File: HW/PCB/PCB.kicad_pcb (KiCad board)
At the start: 2 copper layers, 66.7 x 44 mm, 54 parts, among them J1 USB4105-GF-A, J4 Micro_SD_Card_Det_Hirose_DM3AT, Q1 2PC4081R, Q2 2PC4081R, SW1 ssss213202, SW2 SKRPACE010, SW3 SKRPACE010, U1 BME280, U2 FT231XS, U3 LT1963ES8-3.3, U4 ESP32-S3-WROOM-1, U5 SCD40, U6 AQM0802A-RN-GBW, U7 TPS2065DDBVR, Y1 FC-135

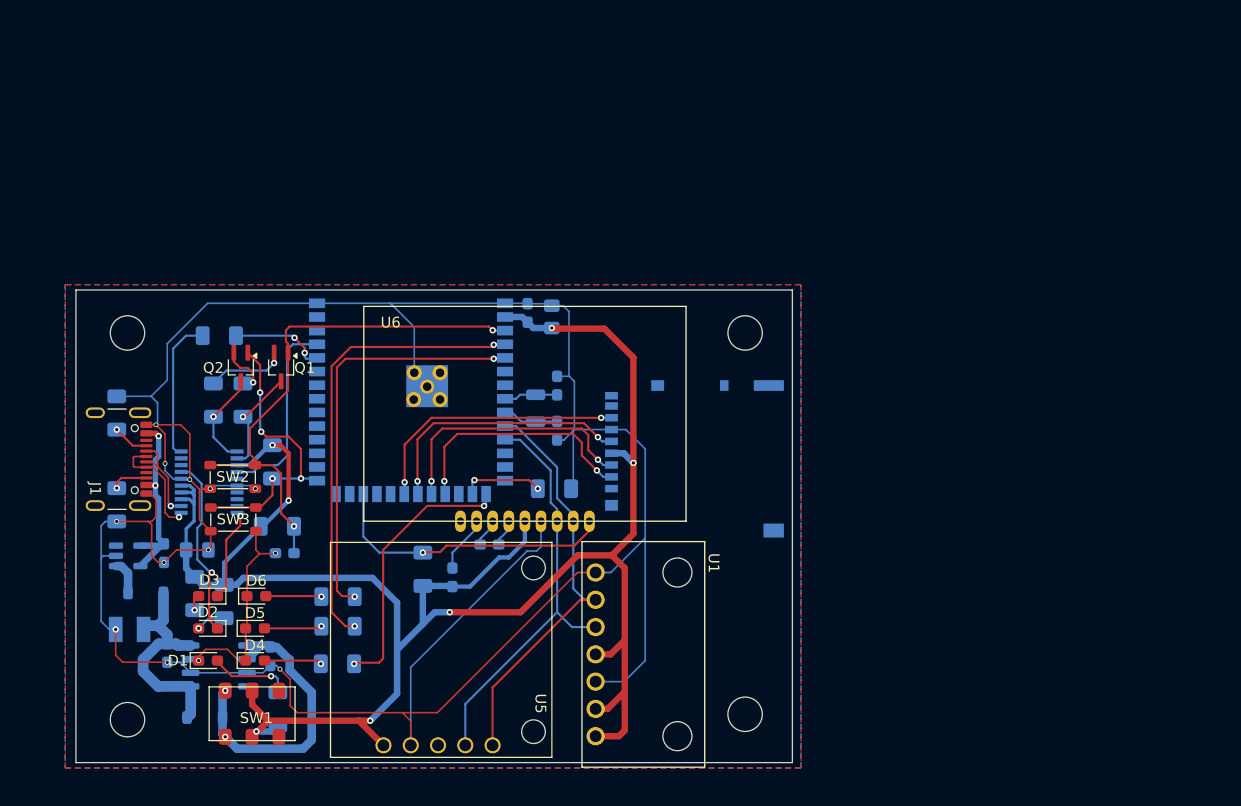
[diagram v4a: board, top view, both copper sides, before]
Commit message: add e-paper module
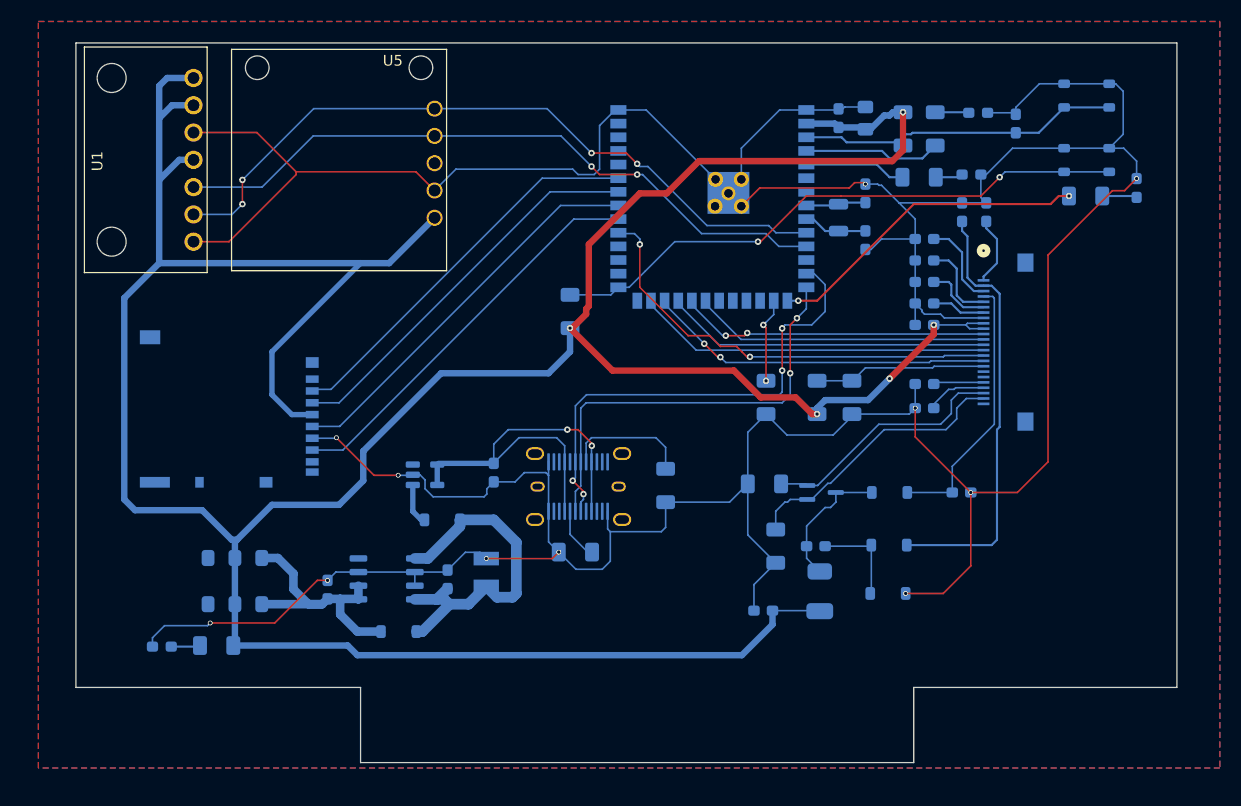
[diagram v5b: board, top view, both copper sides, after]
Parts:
- removed H1, H2, H3, H4: M3_MountHoll, MountingHole:MountingHole_3.2mm_M3
- removed Q1: 2PC4081R, Package_TO_SOT_SMD:SOT-323_SC-70_Handsoldering
- removed R12, R8: 10K, Resistor_SMD:R_1206_3216Metric_Pad1.30x1.75mm_HandSolder
- removed U6: AQM0802A-RN-GBW, mylib:AQM0802A-RN-GBW
- added C13: 4.7uF, Capacitor_SMD:C_0603_1608Metric_Pad1.08x0.95mm_HandSolder, B.Cu at (167.5, 67.2)
- added C15: 4.7uF, Capacitor_SMD:C_0603_1608Metric_Pad1.08x0.95mm_HandSolder, B.Cu at (167.5, 65.2)
- added C16: 4.7uF, Capacitor_SMD:C_0603_1608Metric_Pad1.08x0.95mm_HandSolder, B.Cu at (171.0, 62.8)
- added C17: 1uF, Capacitor_SMD:C_0603_1608Metric_Pad1.08x0.95mm_HandSolder, B.Cu at (173.2, 62.8)
- added C18: 4.7uF, Capacitor_SMD:C_0603_1608Metric_Pad1.08x0.95mm_HandSolder, B.Cu at (152.5, 99.8)
- added C19: 1uF, Capacitor_SMD:C_0603_1608Metric_Pad1.08x0.95mm_HandSolder, B.Cu at (157.4, 93.8)
- added C20: 4.7uF, Capacitor_SMD:C_0603_1608Metric_Pad1.08x0.95mm_HandSolder, B.Cu at (170.9, 88.8)
- added C21: 4.7uF, Capacitor_SMD:C_0603_1608Metric_Pad1.08x0.95mm_HandSolder, B.Cu at (167.5, 81.0)
- added C22: 1uF, Capacitor_SMD:C_0603_1608Metric_Pad1.08x0.95mm_HandSolder, B.Cu at (167.5, 69.2)
- added D9: RB161MM-20, Diode_SMD:D_SOD-123, B.Cu at (164.1, 98.2)
- added L1: 10uH, mylib:AMP10420ED, B.Cu at (157.8, 98.0)
- C3: value 0.1uF -> 4.7uF; footprint Capacitor_SMD:C_0805_2012Metric_Pad1.18x1.45mm_HandSolder -> Capacitor_SMD:C_0603_1608Metric_Pad1.08x0.95mm_HandSolder
- D1, D4, D5, D6, SW1, SW2, SW3: moved to B.Cu
- D2, D3: value LED -> RB161MM-20; footprint LED_SMD:LED_0603_1608Metric_Pad1.05x0.95mm_HandSolder -> Diode_SMD:D_SOD-123; moved to B.Cu
- J1: footprint Connector_USB:USB_C_Receptacle_GCT_USB4105-xx-A_16P_TopMnt_Horizontal -> mylib:USB-C31-S-VT-CS4-BK-PP-TR; moved to B.Cu
- Q2: value 2PC4081R -> SI1308EDL-T1-GE3; moved to B.Cu
- R3: value 470 -> 0.47
- R6: value 10K -> 3
- U2: value FT231XS -> E-Paper; footprint Package_SO:SSOP-20_3.9x8.7mm_P0.635mm -> XF2M-2415-1A:CONN_XF2M-2415-1A_OMR
- moved D4 93.1 mm to (187.2, 60.5), turned to -90 degrees
- moved SW2 87.1 mm to (182.6, 51.9)
- moved SW3 86.2 mm to (182.6, 57.9)
- moved D5 82.7 mm to (172.5, 53.5), turned to 180 degrees
- moved R13 82.1 mm to (182.5, 61.2), turned to 180 degrees
- moved C6 78.9 mm to (176.0, 54.5), turned to 90 degrees
- moved D6 77.3 mm to (171.9, 59.2), turned to 180 degrees
- moved U2 72.5 mm to (173.0, 80.6), turned to -90 degrees
- moved R14 72.4 mm to (168.5, 55.0), turned to -90 degrees
- moved C3 69.4 mm to (167.5, 78.8)
- moved R9 69.0 mm to (165.5, 55.0), turned to 90 degrees
- moved R15 66.7 mm to (167.0, 59.5), turned to 180 degrees
- moved D2 64.7 mm to (164.2, 88.8)
- moved R6 63.9 mm to (160.8, 80.0)
- moved D3 63.6 mm to (164.2, 93.8), turned to 0 degrees
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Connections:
- C10 pad 1: Net-(U6-CAP1N) -> GND
- C10 pad 2: Net-(U6-CAP1P) -> Net-(U2-VDD)
- C3 pad 1: +3V3 -> GND
- C3 pad 2: GND -> Net-(U2-VGH)
- C9 pad 1: +3V3 -> GND
- C9 pad 2: Net-(U6-VOUT) -> +3V3
- D2 pad 1: CBUS1 -> EPAPER_VGH
- D3 pad 1: CBUS2 -> Net-(D3-K)
- D3 pad 2: Net-(D3-A) -> EPAPER_VGL
- J1 pad A6: USB_DP -> ESP32_IO20
- J1 pad A7: USB_DM -> ESP32_IO19
- J1 pad B6: USB_DP -> ESP32_IO20
- J1 pad B7: USB_DM -> ESP32_IO19
- J4 pad 2: ESP32_IO10_SPI_CS -> ESP32_IO42_SD_CS
- J4 pad 3: ESP32_IO11_SPI_MOSI -> ESP32_IO41_SD_MOSI
- J4 pad 5: ESP32_IO12_SPI_SCK -> ESP32_IO40_SD_SCK
- J4 pad 7: ESP32_IO13_SPI_MISO -> ESP32_IO39_SD_MISO
- Q2 pad 1: ESP32_IO0 -> EPAPER_GDR
- Q2 pad 2: Net-(Q2-B) -> EPAPER_RESET
- Q2 pad 3: DTR -> Net-(D2-A)
- R3 pad 1: Net-(U2-TXD) -> EPAPER_RESET
- R3 pad 2: ESP32_RXD -> GND
- R5 pad 1: Net-(D2-A) -> EPAPER_GDR
- R5 pad 2: +3V3 -> GND
- R6 pad 1: Net-(D3-A) -> GND
- R6 pad 2: +3V3 -> Net-(U2-BS)
- R7 pad 1: Net-(Q1-B) -> +3V3
- R7 pad 2: DTR -> Net-(U2-BS)
- U2 pad 1: DTR -> unconnected-(U2-HLT_CTL-Pad1)
- U2 pad 10: CBUS2 -> ESP32_IO38_EPAPER_RST
- U2 pad 11: USB_DP -> ESP32_IO48_EPAPER_DC
- U2 pad 12: USB_DM -> ESP32_IO21_EPAPER_CS
- U2 pad 13: +3V3 -> ESP32_IO14_EPAPER_SCK
- U2 pad 14: +3V3 -> ESP32_IO13_EPAPER_MOSI
- U2 pad 16: GND -> +3V3
- U2 pad 17: CBUS1 -> GND
- U2 pad 18: unconnected-(U2-CBUS0-Pad18) -> Net-(U2-VDD)
- U2 pad 19: unconnected-(U2-CBUS3-Pad19) -> Net-(U2-VPP)
- U2 pad 2: RTS -> EPAPER_GDR
- U2 pad 20: Net-(U2-TXD) -> Net-(U2-VSH)
- U2 pad 3: +3V3 -> EPAPER_RESET
- U2 pad 4: ESP32_TXD -> Net-(U2-VGL)
- U2 pad 5: unconnected-(U2-~{RI}-Pad5) -> Net-(U2-VGH)
- U2 pad 6: GND -> unconnected-(U2-TSCL-Pad6)
- U2 pad 8: unconnected-(U2-~{DCD}-Pad8) -> Net-(U2-BS)
- U2 pad 9: unconnected-(U2-~{CTS}-Pad9) -> ESP32_IO47_EPAPER_BUSY
- U4 pad 13: unconnected-(U4-IO19-Pad13) -> ESP32_IO19
- U4 pad 14: unconnected-(U4-IO20-Pad14) -> ESP32_IO20
- U4 pad 18: ESP32_IO10_SPI_CS -> unconnected-(U4-IO10-Pad18)
- U4 pad 19: ESP32_IO11_SPI_MOSI -> unconnected-(U4-IO11-Pad19)
- U4 pad 20: ESP32_IO12_SPI_SCK -> unconnected-(U4-IO12-Pad20)
- U4 pad 21: ESP32_IO13_SPI_MISO -> ESP32_IO14_EPAPER_SCK
- U4 pad 22: unconnected-(U4-IO14-Pad22) -> ESP32_IO13_EPAPER_MOSI
- U4 pad 23: unconnected-(U4-IO21-Pad23) -> ESP32_IO21_EPAPER_CS
- U4 pad 24: ESP32_IO47 -> ESP32_IO47_EPAPER_BUSY
- U4 pad 25: unconnected-(U4-IO48-Pad25) -> ESP32_IO48_EPAPER_DC
- U4 pad 31: unconnected-(U4-IO38-Pad31) -> ESP32_IO38_EPAPER_RST
- U4 pad 32: unconnected-(U4-IO39-Pad32) -> ESP32_IO39_SD_MISO
- U4 pad 33: unconnected-(U4-IO40-Pad33) -> ESP32_IO40_SD_SCK
- U4 pad 34: unconnected-(U4-IO41-Pad34) -> ESP32_IO41_SD_MOSI
- U4 pad 35: unconnected-(U4-IO42-Pad35) -> ESP32_IO42_SD_CS
- U4 pad 36: ESP32_RXD -> unconnected-(U4-RXD0-Pad36)
- U4 pad 37: ESP32_TXD -> unconnected-(U4-TXD0-Pad37)
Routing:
- net +3V3: track 189.8 -> 323.8 mm, vias 7 -> 5
- net GND: track 284.7 -> 384.2 mm, vias 13 -> 11
- net ESP32_IO19: track 0.00 -> 45.5 mm, vias 0 -> 4
- net ESP32_IO38_EPAPER_RST: track 0.00 -> 41.5 mm, vias 0 -> 2
- net EPAPER_VGL: track 0.00 -> 40.7 mm
- net ESP32_IO20: track 0.00 -> 40.4 mm, vias 0 -> 2
- net ESP32_IO39_SD_MISO: track 0.00 -> 37.4 mm
- net ESP32_IO40_SD_SCK: track 0.00 -> 37.0 mm
- net ESP32_IO42_SD_CS: track 0.00 -> 36.7 mm
- net ESP32_IO41_SD_MOSI: track 0.00 -> 36.6 mm
- net ESP32_IO48_EPAPER_DC: track 0.00 -> 33.1 mm
- net ESP32_IO47_EPAPER_BUSY: track 0.00 -> 32.3 mm, vias 0 -> 2
- net ESP32_IO21_EPAPER_CS: track 0.00 -> 30.3 mm
- net ESP32_IO4: track 42.6 -> 12.8 mm, vias 2 -> 0
- net ESP32_IO5: track 38.7 -> 9.44 mm, vias 2 -> 0
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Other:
- board size 66.7 x 44 mm -> 102.5 x 67 mm

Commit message: modify schematics
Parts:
- removed U3: LT1963ES8-3.3, Package_SO:Infineon_PG-DSO-8-24_4x5mm
- added U6: AZ1117CH-3_3TRG1, Package_TO_SOT_SMD:SOT-223, B.Cu at (115.5, 97.0)
- C2: value 10uF -> 22uF
- moved D7 13.8 mm to (106.0, 96.0), turned to -90 degrees
- moved C1 5.70 mm to (109.0, 93.0)
- moved SW1 5.41 mm to (100.5, 96.0)
- moved C2 2.92 mm to (122.0, 99.6), turned to -90 degrees
- moved C12 1.81 mm to (128.5, 96.5), turned to 0 degrees
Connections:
- C1 pad 1: SW_1 -> VDD
- C2 pad 1: VDD -> SW_1
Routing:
- net GND: track 384.2 -> 341.3 mm, vias 11 -> 8
- net +3V3: track 323.8 -> 284.7 mm
- net VDD: track 33.3 -> 0.00 mm
- net SW_1: track 24.7 -> 0.00 mm
- removed copper zone on B.Cu, net GND
- removed copper zone on F.Cu, net GND

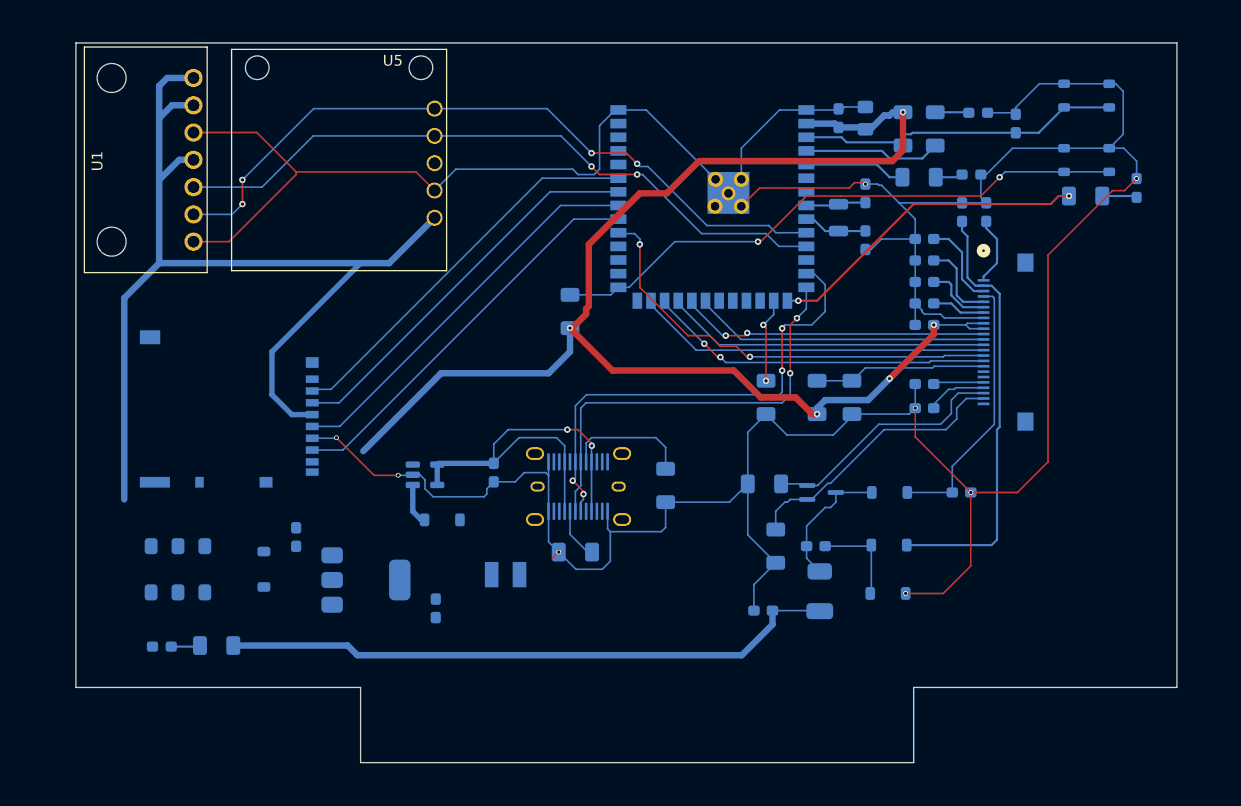
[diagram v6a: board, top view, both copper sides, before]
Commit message: modify PCB layout
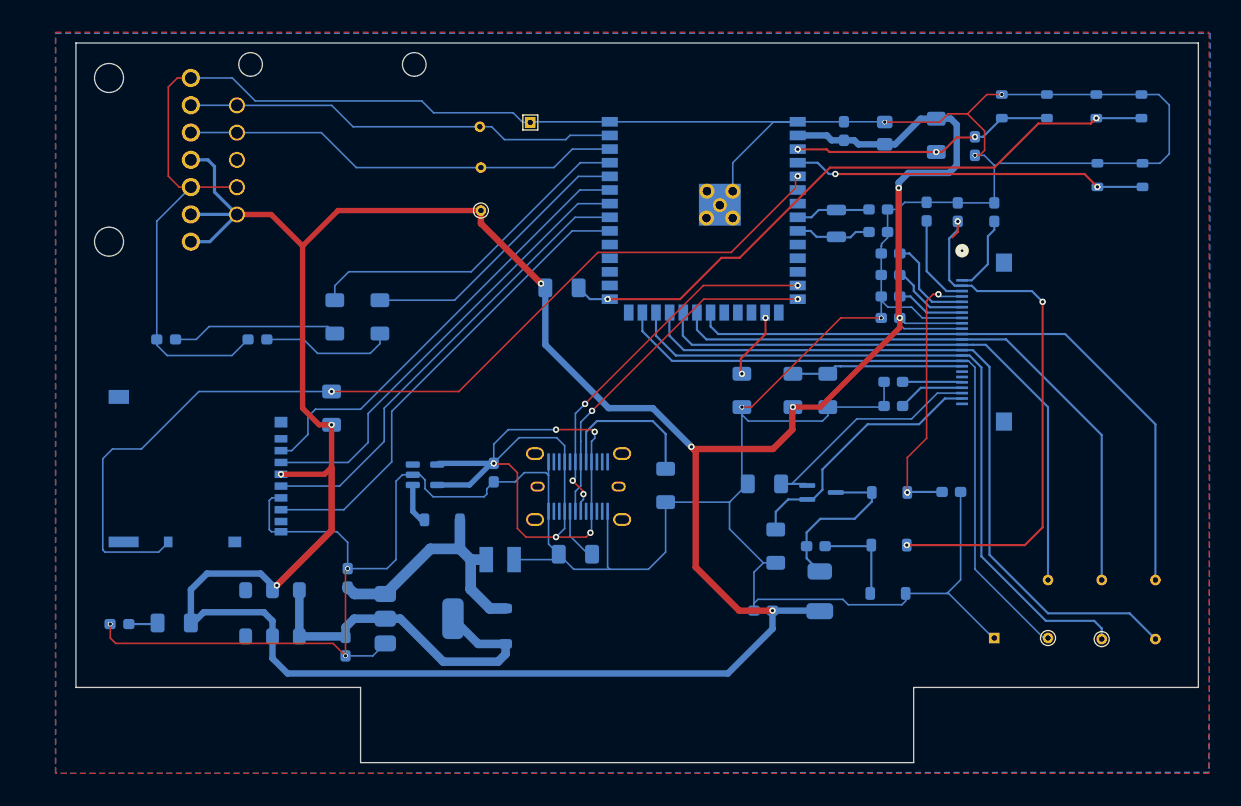
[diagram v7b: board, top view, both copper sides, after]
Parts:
- removed D4: LED, LED_SMD:LED_0603_1608Metric_Pad1.05x0.95mm_HandSolder
- removed R13: 10K, Resistor_SMD:R_1206_3216Metric_Pad1.30x1.75mm_HandSolder
- added R8: 50K, Resistor_SMD:R_1206_3216Metric_Pad1.30x1.75mm_HandSolder, B.Cu at (112.3, 81.0)
- added SW4: SKRPACE010, mylib:SKRPACE010, B.Cu at (185.7, 59.3)
- added TP1: GND, TestPoint:TestPoint_THTPad_1.0x1.0mm_Drill0.5mm, B.Cu at (174.0, 102.4)
- added TP10: 3V3, TestPoint:TestPoint_THTPad_D1.0mm_Drill0.5mm, F.Cu at (126.2, 62.6)
- added TP11: GND, TestPoint:TestPoint_THTPad_1.0x1.0mm_Drill0.5mm, F.Cu at (130.8, 54.4)
- added TP2: BUSY, TestPoint:TestPoint_THTPad_D1.0mm_Drill0.5mm, F.Cu at (179.0, 102.4)
- added TP3: RST, TestPoint:TestPoint_THTPad_D1.0mm_Drill0.5mm, F.Cu at (184.0, 102.5)
- added TP4: D/C, TestPoint:TestPoint_THTPad_D1.0mm_Drill0.5mm, B.Cu at (189.0, 102.5)
- added TP5: CS, TestPoint:TestPoint_THTPad_D1.0mm_Drill0.5mm, B.Cu at (179.0, 97.0)
- added TP6: SCK, TestPoint:TestPoint_THTPad_D1.0mm_Drill0.5mm, B.Cu at (184.0, 97.0)
- added TP7: MOSI, TestPoint:TestPoint_THTPad_D1.0mm_Drill0.5mm, B.Cu at (189.0, 97.0)
- added TP8: SCL, TestPoint:TestPoint_THTPad_D1.0mm_Drill0.5mm, B.Cu at (126.1, 54.8)
- added TP9: SDA, TestPoint:TestPoint_THTPad_D1.0mm_Drill0.5mm, B.Cu at (126.2, 58.6)
- C19: value 1uF -> 4.7uF
- U1, U5: moved to B.Cu
- U2: value E-Paper -> E-Paper 4.26inch, 800x480
- moved D5 78.5 mm to (96.9, 74.6), turned to 0 degrees
- moved D6 68.2 mm to (105.4, 74.6), turned to 0 degrees
- moved R14 58.6 mm to (112.6, 72.5), turned to 90 degrees
- moved R15 51.9 mm to (116.8, 72.5), turned to 90 degrees
- moved D7 23.1 mm to (128.5, 101.3)
- moved U5 18.4 mm to (103.5, 57.9), turned to 180 degrees
- moved SW1 9.71 mm to (109.3, 100.1)
- moved C2 9.12 mm to (113.6, 103.2)
- moved J4 6.27 mm to (99.9, 86.6)
- moved C1 6.12 mm to (113.8, 96.8)
- moved U6 6.12 mm to (120.5, 100.6)
- moved SW2 5.89 mm to (176.8, 52.9)
- moved SW3 5.83 mm to (185.6, 52.9)
- moved D1 4.47 mm to (92.5, 101.1)
- moved R4 4.47 mm to (97.7, 101.0)
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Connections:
- net EPAPER_VGH renamed EPAPER_PREVGH
- net EPAPER_VGL renamed EPAPER_PREVGL
- net ESP32_IO14_EPAPER_SCK renamed ESP32_IO13_EPAPER_SCK
- J4 pad 10: unconnected-(J4-DET_A-Pad10) -> ESP32_IO05_SD_SW
- J4 pad 9: unconnected-(J4-DET_B-Pad9) -> GND
- R14 pad 2: ESP32_IO4 -> ESP32_IO37
- R15 pad 2: ESP32_IO5 -> ESP32_IO36
- U1 pad 2: ESP32_IO17_SCL -> ESP32_IO01_SCL
- U1 pad 3: ESP32_IO18_SDA -> ESP32_IO02_SDA
- U2 pad 10: ESP32_IO38_EPAPER_RST -> ESP32_IO47_EPAPER_RST
- U2 pad 11: ESP32_IO48_EPAPER_DC -> ESP32_IO21_EPAPER_DC
- U2 pad 12: ESP32_IO21_EPAPER_CS -> ESP32_IO14_EPAPER_CS
- U2 pad 14: ESP32_IO13_EPAPER_MOSI -> ESP32_IO12_EPAPER_MOSI
- U2 pad 9: ESP32_IO47_EPAPER_BUSY -> ESP32_IO48_EPAPER_BUSY
- U4 pad 10: ESP32_IO17_SCL -> unconnected-(U4-IO17-Pad10)
- U4 pad 11: ESP32_IO18_SDA -> unconnected-(U4-IO18-Pad11)
- U4 pad 15: ESP32_IO3 -> unconnected-(U4-IO3-Pad15)
- U4 pad 20: unconnected-(U4-IO12-Pad20) -> ESP32_IO12_EPAPER_MOSI
- U4 pad 22: ESP32_IO13_EPAPER_MOSI -> ESP32_IO14_EPAPER_CS
- U4 pad 23: ESP32_IO21_EPAPER_CS -> ESP32_IO21_EPAPER_DC
- U4 pad 24: ESP32_IO47_EPAPER_BUSY -> ESP32_IO47_EPAPER_RST
- U4 pad 25: ESP32_IO48_EPAPER_DC -> ESP32_IO48_EPAPER_BUSY
- U4 pad 31: ESP32_IO38_EPAPER_RST -> unconnected-(U4-IO38-Pad31)
- U4 pad 36: unconnected-(U4-RXD0-Pad36) -> ESP32_IO36
- U4 pad 37: unconnected-(U4-TXD0-Pad37) -> ESP32_IO37
- U4 pad 38: unconnected-(U4-IO2-Pad38) -> ESP32_IO02_SDA
- U4 pad 39: unconnected-(U4-IO1-Pad39) -> ESP32_IO01_SCL
- U4 pad 5: ESP32_IO5 -> ESP32_IO05_SD_SW
- U5 pad 1: ESP32_IO17_SCL -> ESP32_IO01_SCL
- U5 pad 2: ESP32_IO18_SDA -> ESP32_IO02_SDA
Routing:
- net ESP32_IO05_SD_SW: track 0.00 -> 91.4 mm, vias 0 -> 2
- net GND: track 341.3 -> 422.0 mm
- net ESP32_IO21_EPAPER_DC: track 0.00 -> 69.4 mm
- net ESP32_IO17_SCL: track 67.2 -> 0.00 mm, vias 4 -> 0
- net ESP32_IO47_EPAPER_RST: track 0.00 -> 66.2 mm
- net ESP32_IO18_SDA: track 63.3 -> 0.00 mm, vias 2 -> 0
- net ESP32_IO48_EPAPER_BUSY: track 0.00 -> 62.3 mm
- net ESP32_IO12_EPAPER_MOSI: track 0.00 -> 61.0 mm
- net ESP32_IO14_EPAPER_CS: track 0.00 -> 55.0 mm
- net ESP32_IO02_SDA: track 0.00 -> 41.9 mm
- net ESP32_IO38_EPAPER_RST: track 41.5 -> 0.00 mm, vias 2 -> 0
- net ESP32_IO01_SCL: track 0.00 -> 40.7 mm
- net SW_1: track 0.00 -> 33.6 mm
- net ESP32_IO48_EPAPER_DC: track 33.1 -> 0.00 mm
- net ESP32_IO47_EPAPER_BUSY: track 32.3 -> 0.00 mm, vias 2 -> 0
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- added copper zone on B.Cu, net GND
- added copper zone on F.Cu, net GND
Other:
- board size 102.5 x 67 mm -> 104.5 x 67 mm
- board text added: "ERROR"
- board text added: "FLASH"
- board text added: "LED1"
- board text added: "OFF"
- board text added: "ON"
- board text added: "POWER"
- board text added: "RESET"
- board text added: "SELECT"

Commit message: Order HW/PCB/ESP32_SmartClock_GBR_ELECROW.zip to Elecrow (#243165)
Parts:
- TP10, TP11, TP2, TP3: moved to B.Cu
- moved R4 2.20 mm to (99.7, 100.2), turned to 90 degrees
- moved D1 1.28 mm to (93.8, 101.2)
- turned TP10 to 180 degrees
- turned TP11 to 180 degrees
- turned TP2 to 180 degrees
- turned TP3 to 180 degrees
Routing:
- net +3V3: track 293.8 -> 283.8 mm
- net Net-(D1-A): track 2.72 -> 5.23 mm
- net EPAPER_PREVGL: track 51.4 -> 49.7 mm, vias 3 -> 2
- net GND: track 422.0 -> 421.3 mm
